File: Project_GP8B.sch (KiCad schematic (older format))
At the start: 11 parts, among them U1 74AHC05, U2 74AHC05, U3 74AHC1G04, U4 74AHC1G04, U5 74AHC05

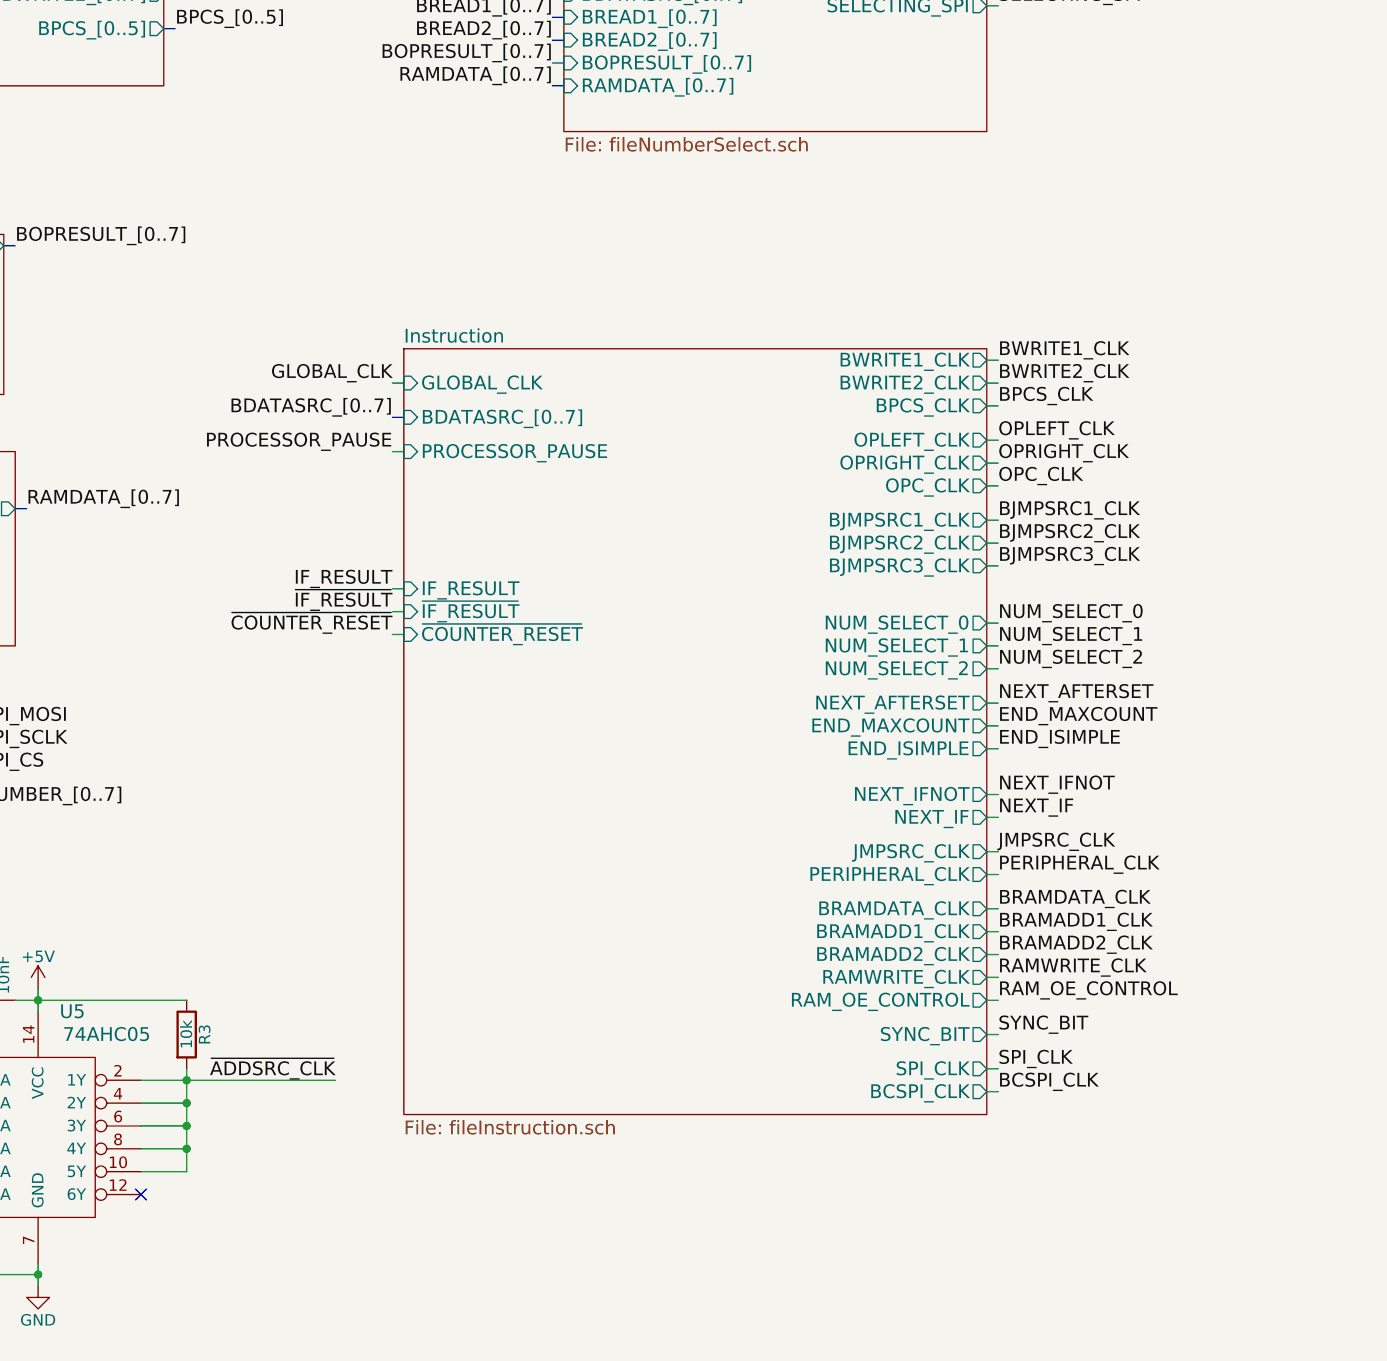
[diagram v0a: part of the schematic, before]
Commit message: Adding copyright and license notice
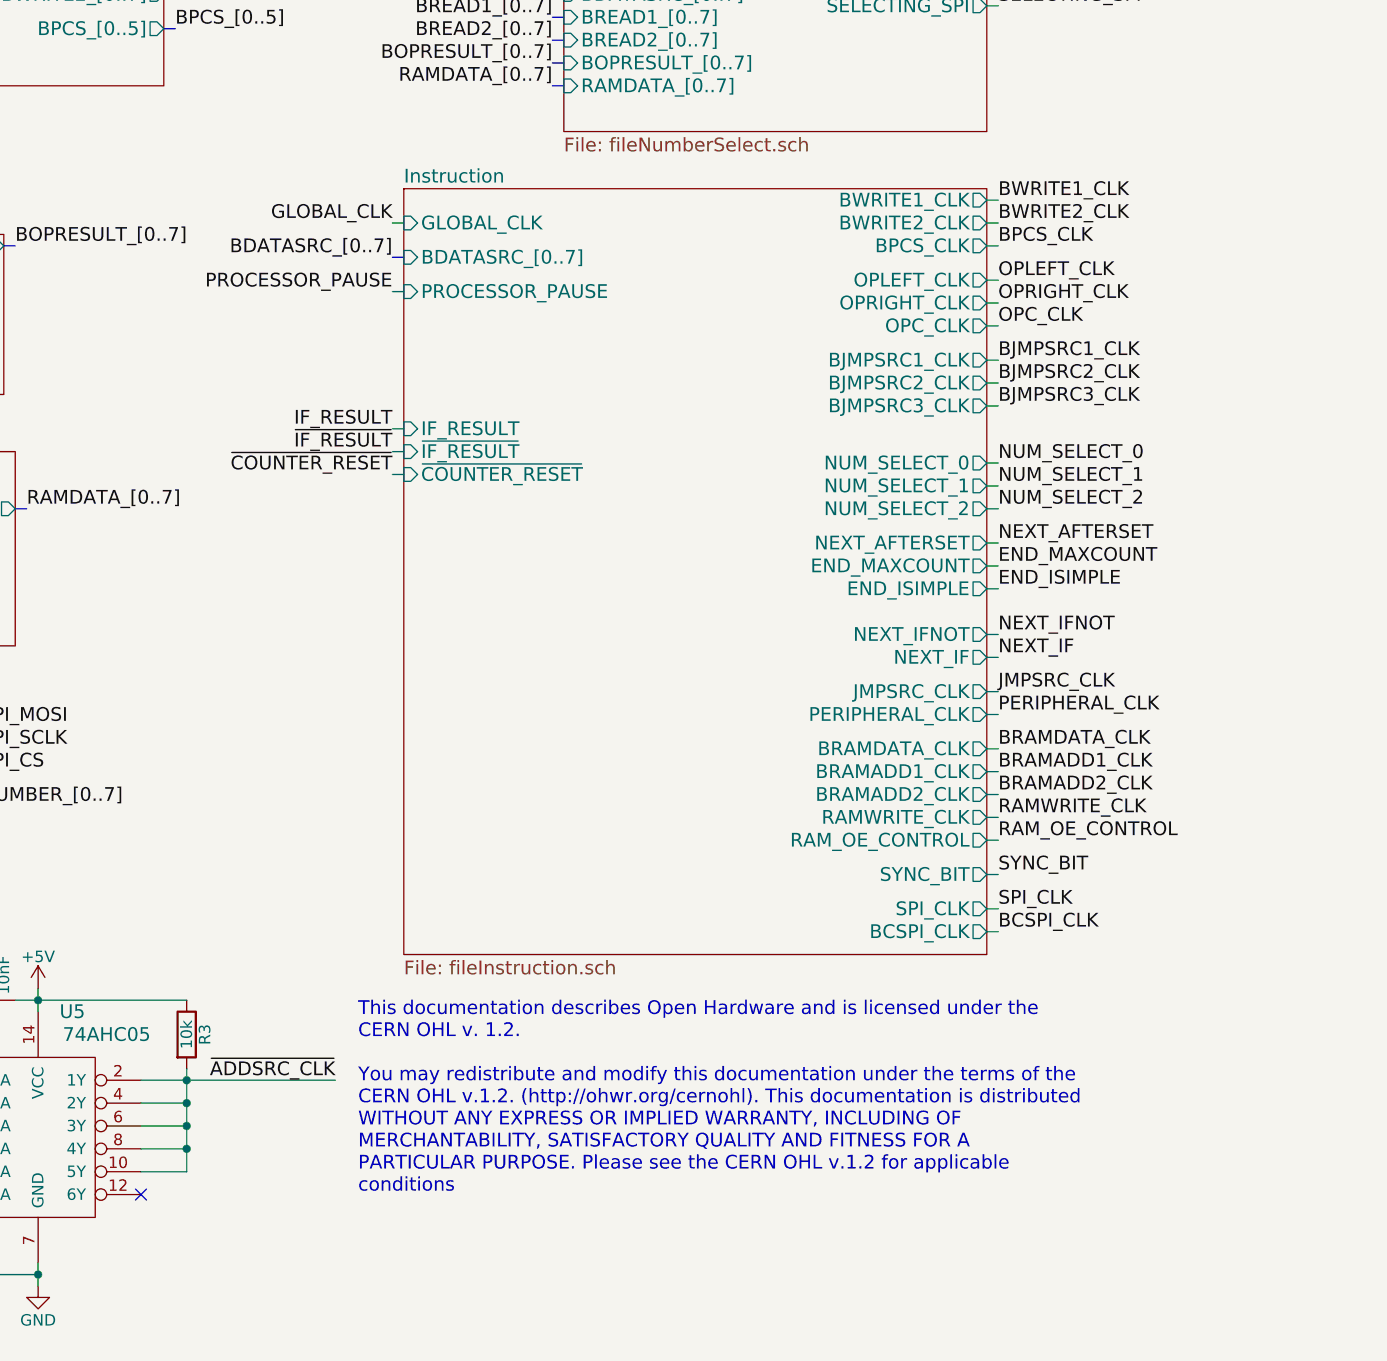
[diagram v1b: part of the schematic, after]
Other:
- note added: "This documentation describes Open Hardware and is licensed under the\nCERN OHL v. 1.2.\n\nYou may redistribute and modify this documentation under the terms of the\nCERN OHL v.1.2. (http://ohwr.org/cernohl). This documentation is distributed\nWITHOUT ANY EXPRESS OR IMPLIED WARRANTY, INCLUDING OF\nMERCHANTABILITY, SATISFACTORY QUALITY AND FITNESS FOR A\nPARTICULAR PURPOSE. Please see the CERN OHL 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"
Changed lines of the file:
@@
 Rev "V4"
 Comp "Guillaume Guillet"
-Comment1 ""
-Comment2 ""
+Comment1 "Copyright Guillaume Guillet 2020"
+Comment2 "Licensed under CERN OHL v.1.2"
 Comment3 ""
 Comment4 ""
@@
 Text Label 10350 900  0    60   ~ 0
 NUMBER_[0..7]
-Text Label 10350 4800 0    60   ~ 0
+Text Label 10350 4100 0    60   ~ 0
 NEXT_IF
-Text Label 10350 3500 0    60   ~ 0
+Text Label 10350 2800 0    60   ~ 0
 BJMPSRC1_CLK
-Text Label 10350 3000 0    60   ~ 0
+Text Label 10350 2300 0    60   ~ 0
 BPCS_CLK
-Text Label 10350 2800 0    60   ~ 0
+Text Label 10350 2100 0    60   ~ 0
 BWRITE1_CLK
+Text Label 10350 2200 0    60   ~ 0
+BWRITE2_CLK
+Text Label 10350 4350 0    60   ~ 0
+PERIPHERAL_CLK
 Text Label 10350 2900 0    60   ~ 0
-BWRITE2_CLK
-Text Label 10350 5050 0    60   ~ 0
-PERIPHERAL_CLK
+BJMPSRC2_CLK
+Text Label 10350 2450 0    60   ~ 0
+OPLEFT_CLK
+Text Label 10350 2550 0    60   ~ 0
+OPRIGHT_CLK
+Text Label 10350 2650 0    60   ~ 0
+OPC_CLK
+Text Label 10350 4000 0    60   ~ 0
+NEXT_IFNOT
+Text Label 10350 3700 0    60   ~ 0
+END_MAXCOUNT
 Text Label 10350 3600 0    60   ~ 0
-BJMPSRC2_CLK
-Text Label 10350 3150 0    60   ~ 0
-OPLEFT_CLK
+NEXT_AFTERSET
 Text Label 10350 3250 0    60   ~ 0
-OPRIGHT_CLK
+NUM_SELECT_0
 Text Label 10350 3350 0    60   ~ 0
-OPC_CLK
-Text Label 10350 4700 0    60   ~ 0
-NEXT_IFNOT
-Text Label 10350 4400 0    60   ~ 0
-END_MAXCOUNT
-Text Label 10350 4300 0    60   ~ 0
-NEXT_AFTERSET
-Text Label 10350 3950 0    60   ~ 0
-NUM_SELECT_0
-Text Label 10350 4050 0    60   ~ 0
 NUM_SELECT_1
-Text Label 7700 2900 2    60   ~ 0
+Text Label 7700 2200 2    60   ~ 0
 GLOBAL_CLK
-Text Label 7700 3800 2    60   ~ 0
+Text Label 7700 3100 2    60   ~ 0
 IF_RESULT
-Text Label 7700 3900 2    60   ~ 0
+Text Label 7700 3200 2    60   ~ 0
 ~IF_RESULT
-Text Label 7700 4000 2    60   ~ 0
+Text Label 7700 3300 2    60   ~ 0
 ~COUNTER_RESET
-Text Label 10350 4500 0    60   ~ 0
+Text Label 10350 3800 0    60   ~ 0
 END_ISIMPLE
 $Comp
@@
 Text Label 3250 1450 0    60   ~ 0
 RESET_CLK
-Text Label 7700 3050 2    60   ~ 0
+Text Label 7700 2350 2    60   ~ 0
 BDATASRC_[0..7]
 $Sheet
@@
 F8 "RAMWRITE_CLK" I L 4200 3850 60
 $EndSheet
-Text Label 10350 5200 0    60   ~ 0
+Text Label 10350 4500 0    60   ~ 0
 BRAMDATA_CLK
-Text Label 10350 5500 0    60   ~ 0
+Text Label 10350 4800 0    60   ~ 0
 RAMWRITE_CLK
-Text Label 10350 5300 0    60   ~ 0
+Text Label 10350 4600 0    60   ~ 0
 BRAMADD1_CLK
-Text Label 10350 5400 0    60   ~ 0
+Text Label 10350 4700 0    60   ~ 0
 BRAMADD2_CLK
-Text Label 10350 5600 0    60   ~ 0
+Text Label 10350 4900 0    60   ~ 0
 RAM_OE_CONTROL
 Text Label 4150 3450 2    60   ~ 0
@@
 Text Label 4950 1500 2    60   ~ 0
 BJMPSRC3_CLK
-Text Label 10350 3700 0    60   ~ 0
+Text Label 10350 3000 0    60   ~ 0
 BJMPSRC3_CLK
-Text Label 10350 5750 0    60   ~ 0
+Text Label 10350 5050 0    60   ~ 0
 SYNC_BIT
 Text Label 1850 3000 0    60   ~ 0
@@
 	900  5300 900  5850
 Connection ~ 900  5850
-Text Label 10350 4150 0    60   ~ 0
+Text Label 10350 3450 0    60   ~ 0
 NUM_SELECT_2
 Text Label 8400 1050 2    60   ~ 0
@@
 	6100 3450 6050 3450
 Wire Bus Line
-	7700 3050 7750 3050
-Wire Wire Line
-	7700 2900 7750 2900
-Wire Wire Line
-	7700 3800 7750 3800
-Wire Wire Line
-	7700 3900 7750 3900
-Wire Wire Line
-	7700 4000 7750 4000
+	7700 2350 7750 2350
+Wire Wire Line
+	7700 2200 7750 2200
+Wire Wire Line
+	7700 3100 7750 3100
+Wire Wire Line
+	7700 3200 7750 3200
+Wire Wire Line
+	7700 3300 7750 3300
+Wire Wire Line
+	10350 2100 10300 2100
+Wire Wire Line
+	10350 2200 10300 2200
+Wire Wire Line
+	10350 2300 10300 2300
+Wire Wire Line
+	10350 2450 10300 2450
+Wire Wire Line
+	10350 2550 10300 2550
+Wire Wire Line
+	10350 2650 10300 2650
 Wire Wire Line
 	10350 2800 10300 2800
@@
 	10350 3000 10300 3000
 Wire Wire Line
-	10350 3150 10300 3150
-Wire Wire Line
 	10350 3250 10300 3250
 Wire Wire Line
 	10350 3350 10300 3350
 Wire Wire Line
-	10350 3500 10300 3500
+	10350 3450 10300 3450
 Wire Wire Line
 	10350 3600 10300 3600
@@
 	10350 3700 10300 3700
 Wire Wire Line
-	10350 3950 10300 3950
-Wire Wire Line
-	10350 4050 10300 4050
-Wire Wire Line
-	10350 4150 10300 4150
-Wire Wire Line
-	10350 4300 10300 4300
-Wire Wire Line
-	10350 4400 10300 4400
+	10350 3800 10300 3800
+Wire Wire Line
+	10350 4000 10300 4000
+Wire Wire Line
+	10350 4100 10300 4100
+Wire Wire Line
+	10350 4250 10300 4250
+Wire Wire Line
+	10350 4350 10300 4350
 Wire Wire Line
 	10350 4500 10300 4500
 Wire Wire Line
+	10350 4600 10300 4600
+Wire Wire Line
 	10350 4700 10300 4700
 Wire Wire Line
 	10350 4800 10300 4800
 Wire Wire Line
-	10350 4950 10300 4950
+	10350 4900 10300 4900
 Wire Wire Line
 	10350 5050 10300 5050
-Wire Wire Line
-	10350 5200 10300 5200
-Wire Wire Line
-	10350 5300 10300 5300
-Wire Wire Line
-	10350 5400 10300 5400
-Wire Wire Line
-	10350 5500 10300 5500
-Wire Wire Line
-	10350 5600 10300 5600
-Wire Wire Line
-	10350 5750 10300 5750
 Wire Wire Line
 	6150 6800 6150 6850
@@
 Text Label 3250 1700 0    60   ~ 0
 PROCESSOR_PAUSE
-Text Label 7700 3200 2    60   ~ 0
+Text Label 7700 2500 2    60   ~ 0
 PROCESSOR_PAUSE
 Wire Wire Line
-	7750 3200 7700 3200
+	7750 2500 7700 2500
 Wire Wire Line
 	6800 5950 7450 5950
 Text Label 4250 2400 2    60   ~ 0
 NUMBER_[0..7]
-Text Label 10350 4950 0    60   ~ 0
+Text Label 10350 4250 0    60   ~ 0
 JMPSRC_CLK
 $Sheet
-S 7750 2750 2550 3350
+S 7750 2050 2550 3350
 U 5ABE9197
 F0 "Instruction" 60
 F1 "fileInstruction.sch" 60
-F2 "GLOBAL_CLK" I L 7750 2900 60
-F3 "IF_RESULT" I L 7750 3800 60
-F4 "~IF_RESULT" I L 7750 3900 60
-F5 "~COUNTER_RESET" I L 7750 4000 60
-F6 "NUM_SELECT_0" O R 10300 3950 60
-F7 "NUM_SELECT_1" O R 10300 4050 60
-F8 "SYNC_BIT" O R 10300 5750 60
-F9 "RAM_OE_CONTROL" O R 10300 5600 60
-F10 "NUM_SELECT_2" O R 10300 4150 60
-F11 "BDATASRC_[0..7]" I L 7750 3050 60
-F12 "PROCESSOR_PAUSE" I L 7750 3200 60
-F13 "BWRITE1_CLK" O R 10300 2800 60
-F14 "BWRITE2_CLK" O R 10300 2900 60
-F15 "BPCS_CLK" O R 10300 3000 60
-F16 "BJMPSRC1_CLK" O R 10300 3500 60
-F17 "BJMPSRC2_CLK" O R 10300 3600 60
-F18 "JMPSRC_CLK" O R 10300 4950 60
-F19 "PERIPHERAL_CLK" O R 10300 5050 60
-F20 "BJMPSRC3_CLK" O R 10300 3700 60
-F21 "SPI_CLK" O R 10300 5900 60
-F22 "OPLEFT_CLK" O R 10300 3150 60
-F23 "OPRIGHT_CLK" O R 10300 3250 60
-F24 "OPC_CLK" O R 10300 3350 60
-F25 "BRAMDATA_CLK" O R 10300 5200 60
-F26 "RAMWRITE_CLK" O R 10300 5500 60
-F27 "BRAMADD2_CLK" O R 10300 5400 60
-F28 "BRAMADD1_CLK" O R 10300 5300 60
-F29 "NEXT_IF" O R 10300 4800 60
-F30 "NEXT_IFNOT" O R 10300 4700 60
-F31 "END_MAXCOUNT" O R 10300 4400 60
-F32 "NEXT_AFTERSET" O R 10300 4300 60
-F33 "END_ISIMPLE" O R 10300 4500 60
-F34 "BCSPI_CLK" O R 10300 6000 60
+F2 "GLOBAL_CLK" I L 7750 2200 60
+F3 "IF_RESULT" I L 7750 3100 60
+F4 "~IF_RESULT" I L 7750 3200 60
+F5 "~COUNTER_RESET" I L 7750 3300 60
+F6 "NUM_SELECT_0" O R 10300 3250 60
+F7 "NUM_SELECT_1" O R 10300 3350 60
+F8 "SYNC_BIT" O R 10300 5050 60
+F9 "RAM_OE_CONTROL" O R 10300 4900 60
+F10 "NUM_SELECT_2" O R 10300 3450 60
+F11 "BDATASRC_[0..7]" I L 7750 2350 60
+F12 "PROCESSOR_PAUSE" I L 7750 2500 60
+F13 "BWRITE1_CLK" O R 10300 2100 60
+F14 "BWRITE2_CLK" O R 10300 2200 60
+F15 "BPCS_CLK" O R 10300 2300 60
+F16 "BJMPSRC1_CLK" O R 10300 2800 60
+F17 "BJMPSRC2_CLK" O R 10300 2900 60
+F18 "JMPSRC_CLK" O R 10300 4250 60
+F19 "PERIPHERAL_CLK" O R 10300 4350 60
+F20 "BJMPSRC3_CLK" O R 10300 3000 60
+F21 "SPI_CLK" O R 10300 5200 60
+F22 "OPLEFT_CLK" O R 10300 2450 60
+F23 "OPRIGHT_CLK" O R 10300 2550 60
+F24 "OPC_CLK" O R 10300 2650 60
+F25 "BRAMDATA_CLK" O R 10300 4500 60
+F26 "RAMWRITE_CLK" O R 10300 4800 60
+F27 "BRAMADD2_CLK" O R 10300 4700 60
+F28 "BRAMADD1_CLK" O R 10300 4600 60
+F29 "NEXT_IF" O R 10300 4100 60
+F30 "NEXT_IFNOT" O R 10300 4000 60
+F31 "END_MAXCOUNT" O R 10300 3700 60
+F32 "NEXT_AFTERSET" O R 10300 3600 60
+F33 "END_ISIMPLE" O R 10300 3800 60
+F34 "BCSPI_CLK" O R 10300 5300 60
 $EndSheet
 Text Label 7450 5950 2    60   ~ 0
@@
 Wire Wire Line
 	1350 2350 1400 2350
-Text Label 10350 5900 0    60   ~ 0
+Text Label 10350 5200 0    60   ~ 0
 SPI_CLK
 Wire Wire Line
-	10350 5900 10300 5900
-Wire Wire Line
-	10300 6000 10350 6000
+	10350 5200 10300 5200
+Wire Wire Line
+	10300 5300 10350 5300
 Text Label 4250 2750 2    60   ~ 0
 OPLEFT_CLK
@@
 Wire Wire Line
 	5650 6800 6150 6800
-Text Label 10350 6000 0    60   ~ 0
+Text Label 10350 5300 0    60   ~ 0
 BCSPI_CLK
+Text Notes 7550 6450 0    60   ~ 0
+This documentation describes Open Hardware and is licensed under the\nCERN OHL v. 1.2.\n\nYou may redistribute and modify this documentation under the terms of the\nCERN OHL v.1.2. (http://ohwr.org/cernohl). This documentation is distributed\nWITHOUT ANY EXPRESS OR IMPLIED WARRANTY, INCLUDING OF\nMERCHANTABILITY, SATISFACTORY QUALITY AND FITNESS FOR A\nPARTICULAR PURPOSE. Please see the CERN OHL v.1.2 for applicable\nconditions
 Wire Bus Line
 	1700 2800 1700 3600
